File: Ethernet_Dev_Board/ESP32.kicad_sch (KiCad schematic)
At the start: 23 parts, among them J401 TAG-CONNECT_NL_10-POS_LEGS, Q401 PMV48XPA2R, Q402 PMV48XPA2R, U401 74AUP1T08GWH, U402 ESP32-WROOM-32E

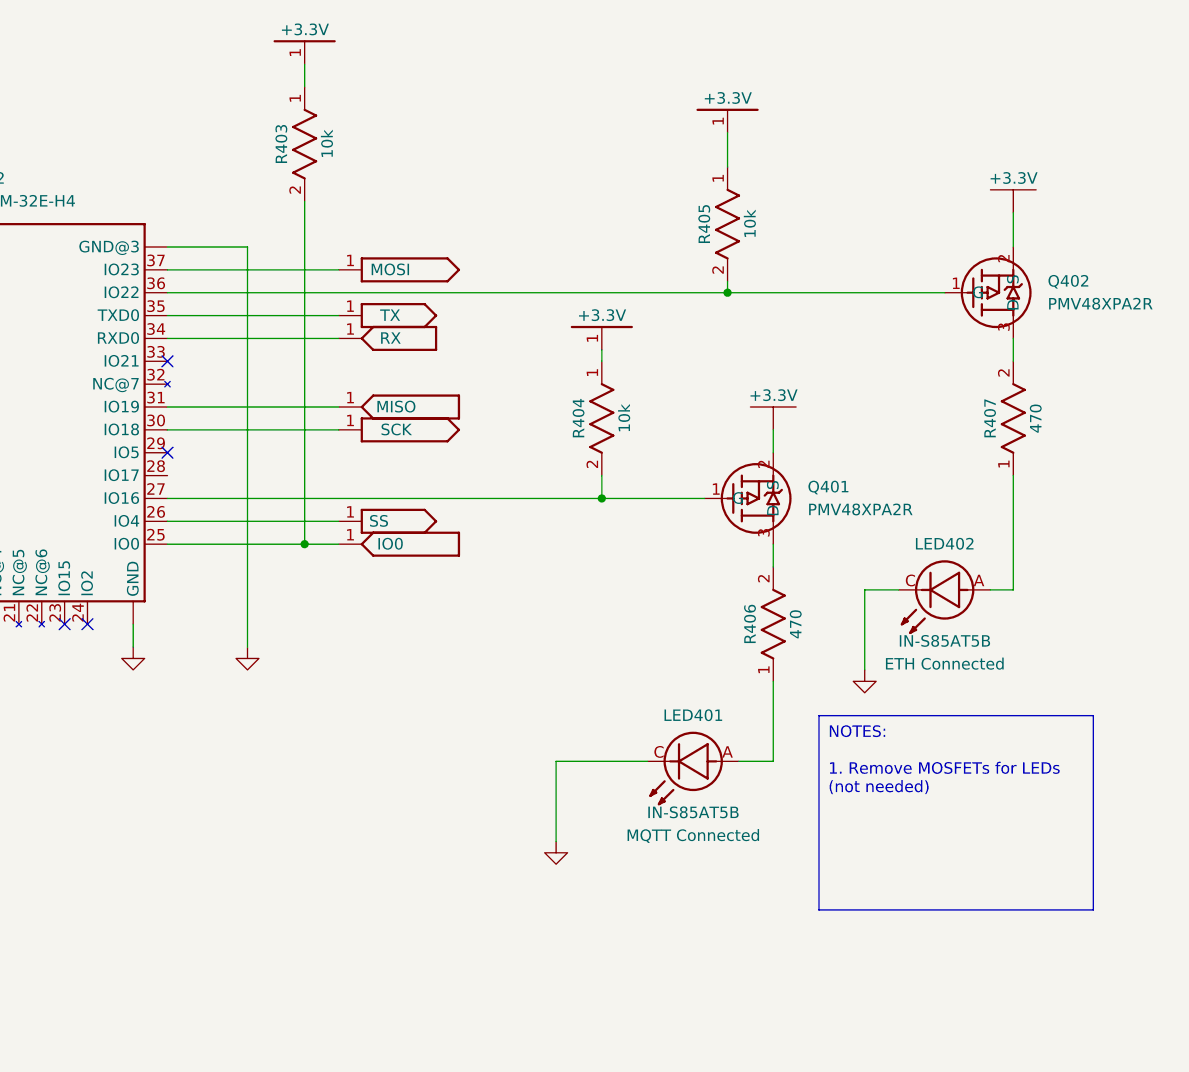
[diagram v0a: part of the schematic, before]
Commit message: Added TVS diode and redid the LED circuit on the ESP32
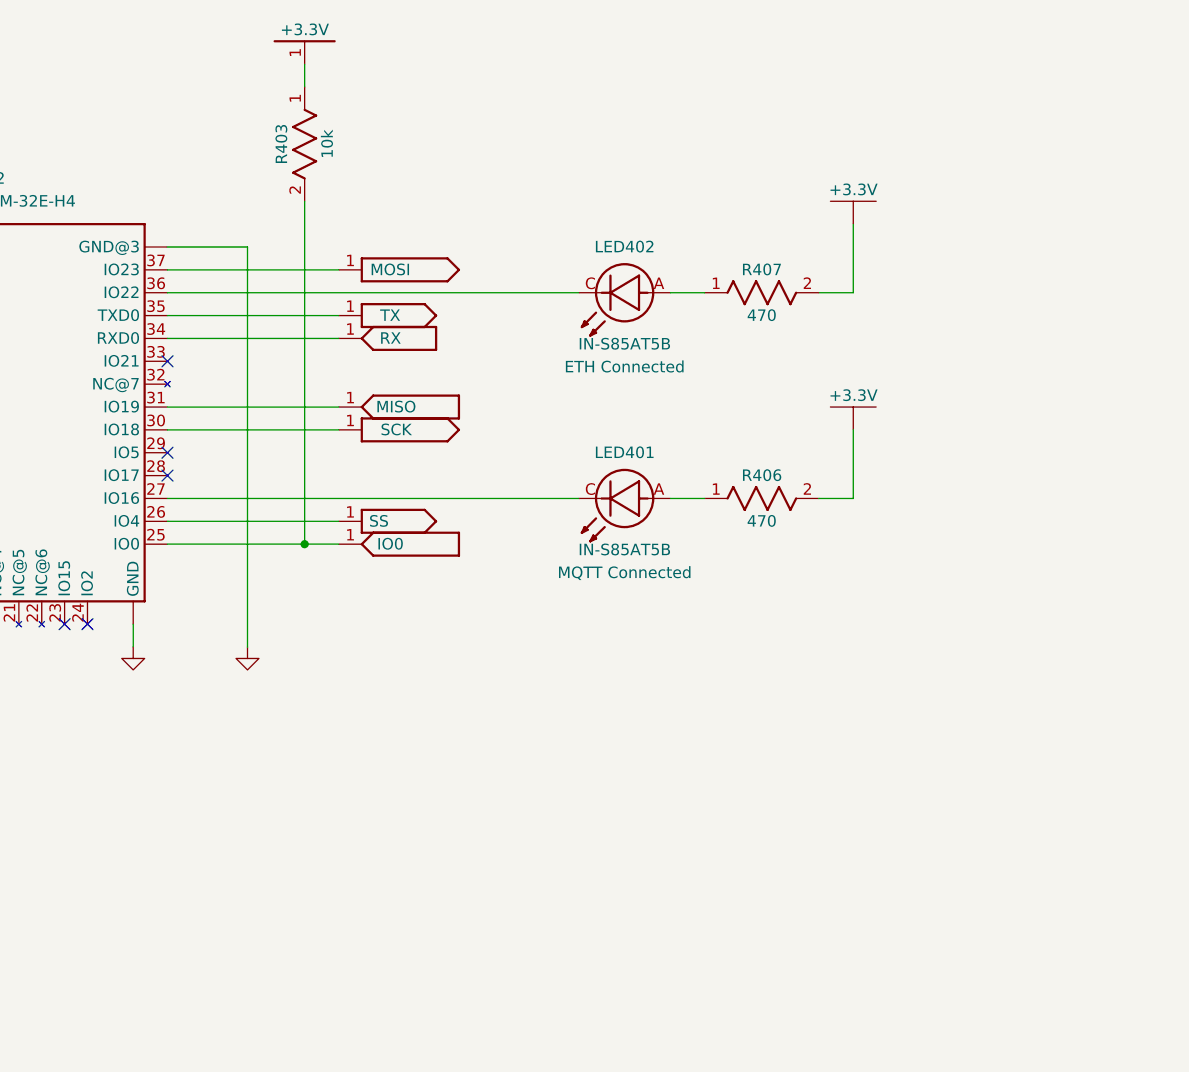
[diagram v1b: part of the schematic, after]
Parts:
- removed Q401, Q402: PMV48XPA2R, RG_TO_SOT_SMD:SOT23-3P95, symbol RG_FETs:PMV48XPA2R
- removed R404, R405: 10k, RG_Resistors_SMD:0603, symbol LED_Controller_Hardware-eagle-import:RES-0603
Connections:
- net +3.3V: now also R406.2, R407.2
- net GNDS: no longer LED401.C, LED402.C
- net at U402.36 (IO22): now also LED402.C
- net at U402.27 (IO16): now also LED401.C
- no-connect marks 19 -> 20
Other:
- moved on the sheet: LED401, LED402, R406, R407
